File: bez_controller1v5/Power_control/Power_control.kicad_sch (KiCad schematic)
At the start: 7 parts, among them J1 Screw_Terminal_01x02, Q2 IRF4905STRLPBF, SW1 GPB040B05BR

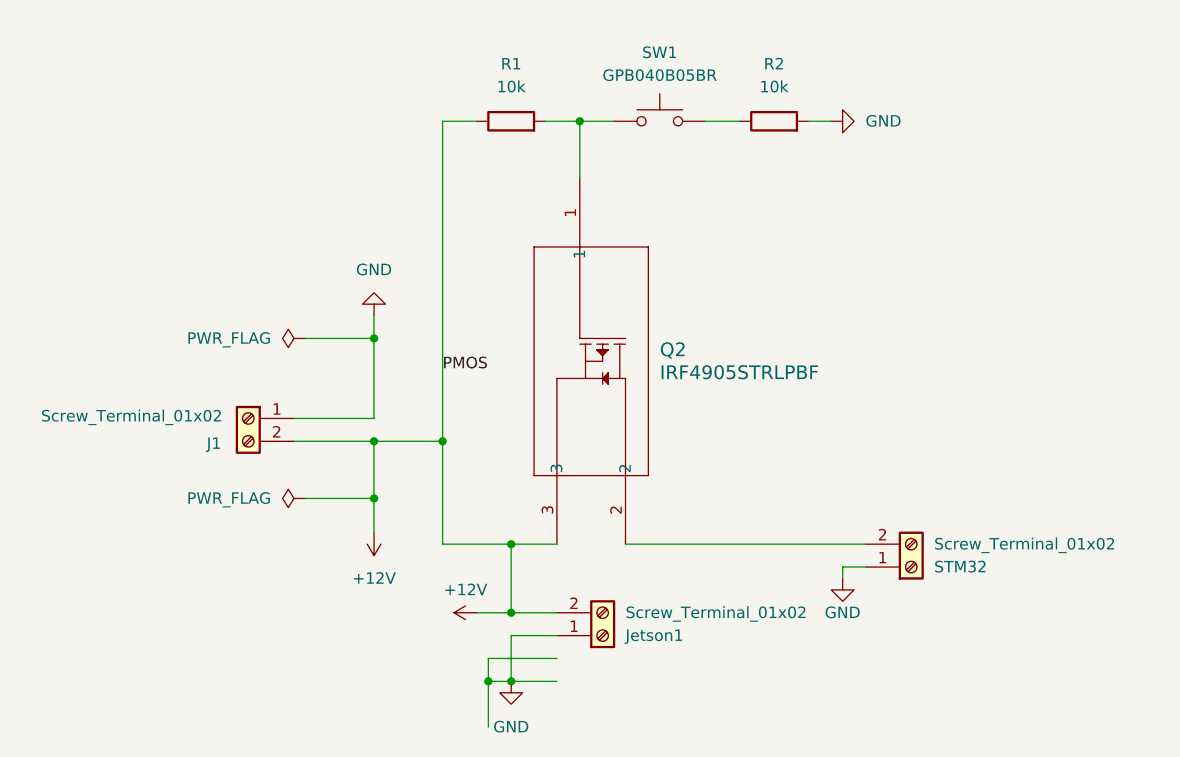
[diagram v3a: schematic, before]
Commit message: Fixed Drain and Source
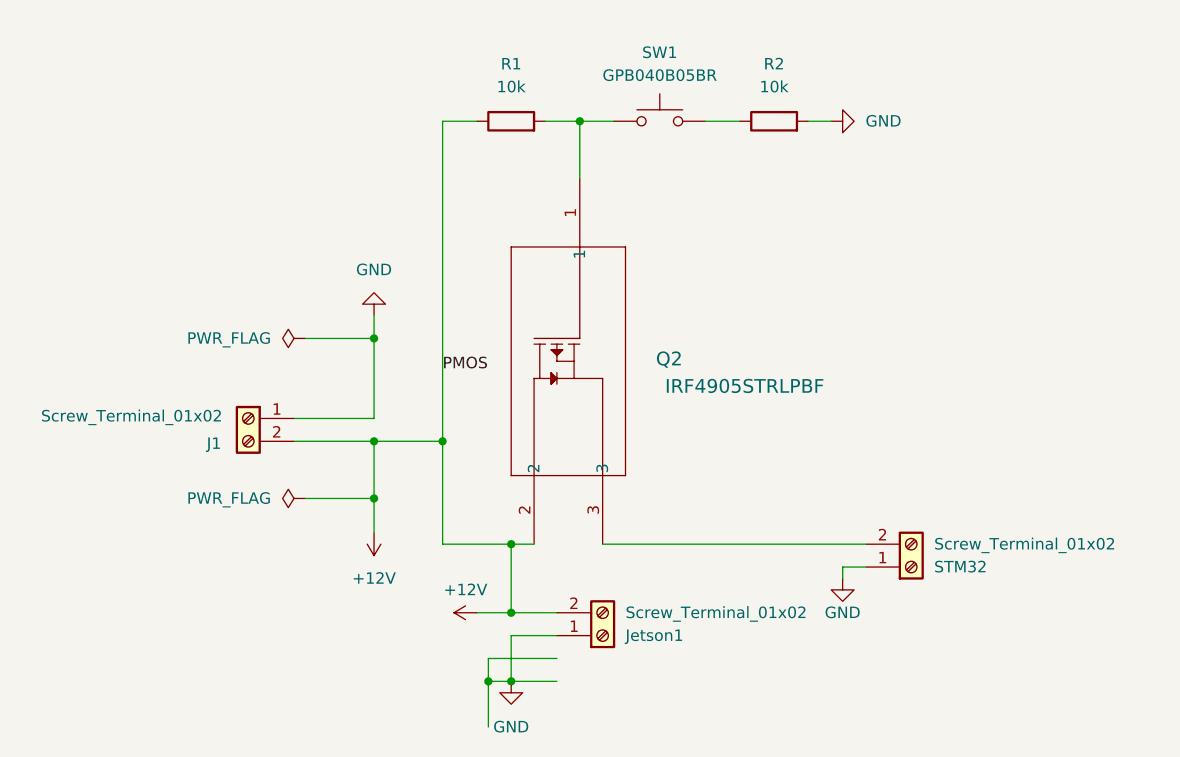
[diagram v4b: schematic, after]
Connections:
- net +12V: now also Q2.2; no longer Q2.3
- net at STM32.2 (Pin_2): now also Q2.3; no longer Q2.2
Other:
- moved on the sheet: Q2
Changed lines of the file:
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@@
+	)
+	(junction
+		(at 85.09 99.06)
+		(diameter 0)
+		(color 0 0 0 0)
 	)
 	(junction
@@
 	)
 	(junction
-		(at 85.09 99.06)
-		(diameter 0)
-		(color 0 0 0 0)
-	)
-	(junction
 		(at 92.71 52.07)
 		(diameter 0)
@@
 	(wire
 		(pts
-			(xy 85.09 99.06) (xy 90.17 99.06)
-		)
-		(stroke
-			(width 0)
-			(type default)
-		)
-	)
-	(wire
-		(pts
 			(xy 85.09 99.06) (xy 85.09 106.68)
 		)
@@
 	(wire
 		(pts
-			(xy 97.79 99.06) (xy 124.46 99.06)
-		)
-		(stroke
-			(width 0)
-			(type default)
-		)
-	)
-	(wire
-		(pts
 			(xy 69.85 93.98) (xy 69.85 97.79)
 		)
@@
 	(wire
 		(pts
+			(xy 95.25 99.06) (xy 124.46 99.06)
+		)
+		(stroke
+			(width 0)
+			(type default)
+		)
+	)
+	(wire
+		(pts
 			(xy 92.71 52.07) (xy 96.52 52.07)
 		)
@@
 		(pts
 			(xy 62.23 76.2) (xy 69.85 76.2)
+		)
+		(stroke
+			(width 0)
+			(type default)
+		)
+	)
+	(wire
+		(pts
+			(xy 85.09 99.06) (xy 87.63 99.06)
 		)
 		(stroke
@@
 	(symbol
 		(lib_id "IRF4905STRLPBF_PMOS:IRF4905STRLPBF")
-		(at 95.25 58.42 270)
+		(at 90.17 58.42 90)
+		(mirror x)
 		(unit 1)
 		(exclude_from_sim no)
@@
 		(dnp no)
 		(property "Reference" "Q2"
-			(at 101.6 77.4699 90)
+			(at 104.14 78.486 90)
 			(effects
 				(font
@@
 		)
 		(property "Value" "IRF4905STRLPBF"
-			(at 101.6 80.0099 90)
+			(at 119.888 81.534 90)
 			(effects
 				(font
@@
 		)
 		(property "Footprint" "Library:IRF4905"
-			(at 95.25 58.42 0)
+			(at 90.17 58.42 0)
 			(effects
 				(font
@@
 		)
 		(property "Datasheet" "IRF4905STRLPBF"
-			(at 95.25 58.42 0)
+			(at 90.17 58.42 0)
 			(effects
 				(font
@@
 		)
 		(property "Description" ""
-			(at 95.25 58.42 0)
-			(effects
-				(font
+			(at 90.17 58.42 0)
+			(effects
+				(font

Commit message: changed battery side XT60 into a vertical one
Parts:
- J1: footprint Connector_AMASS:AMASS_XT60PW-F_1x02_P7.20mm_Horizontal -> xt60:AMASS_XT60-M
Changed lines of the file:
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@@
 			)
 		)
-		(property "Footprint" "Connector_AMASS:AMASS_XT60PW-F_1x02_P7.20mm_Horizontal"
+		(property "Footprint" "xt60:AMASS_XT60-M"
 			(at 55.88 85.09 0)
 			(effects
